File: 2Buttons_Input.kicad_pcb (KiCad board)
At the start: 2 copper layers, 46.2 x 30.2 mm, 19 parts, among them J1 JST_SH_SM06B-SRSS-TB_1x06-1MP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, SW1 SW_Push, SW2 SW_Push, U1 M24C02-FMN

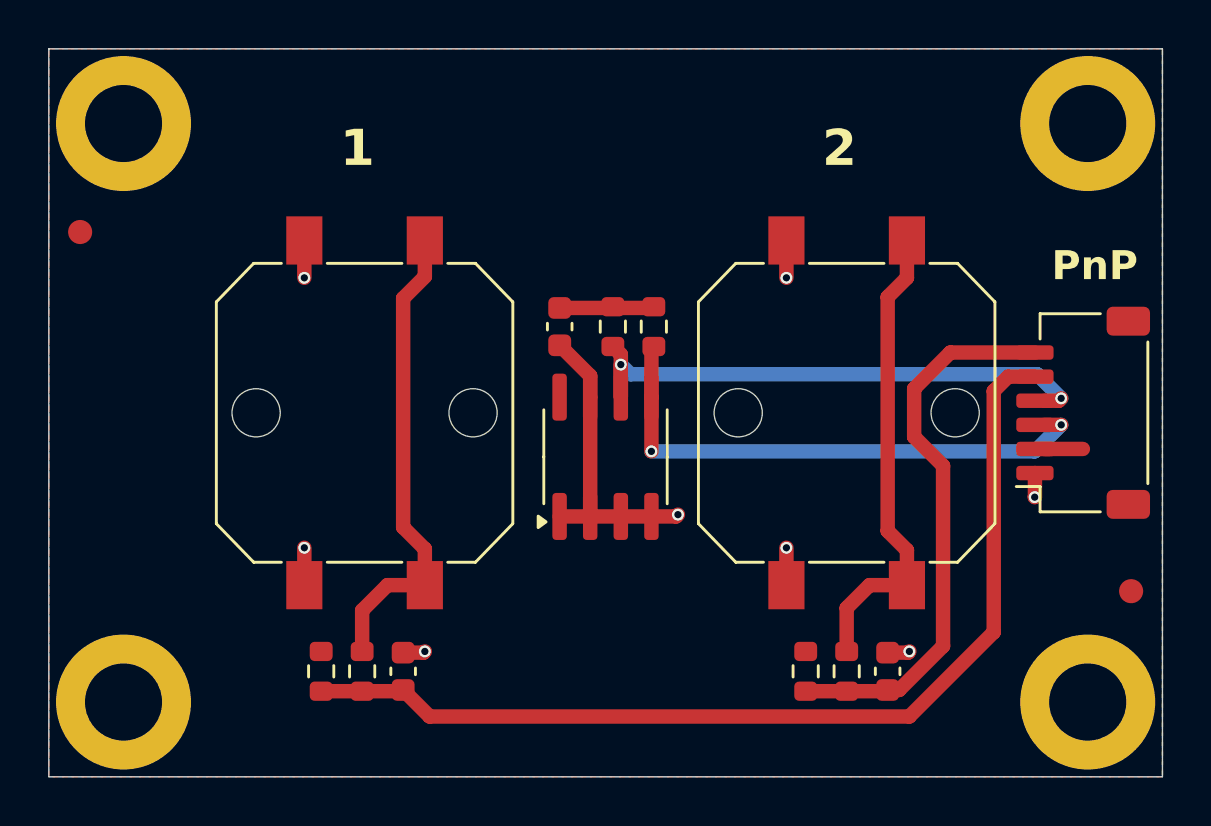
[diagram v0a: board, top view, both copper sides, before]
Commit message: Changing the button names on silk level to 0 and 1
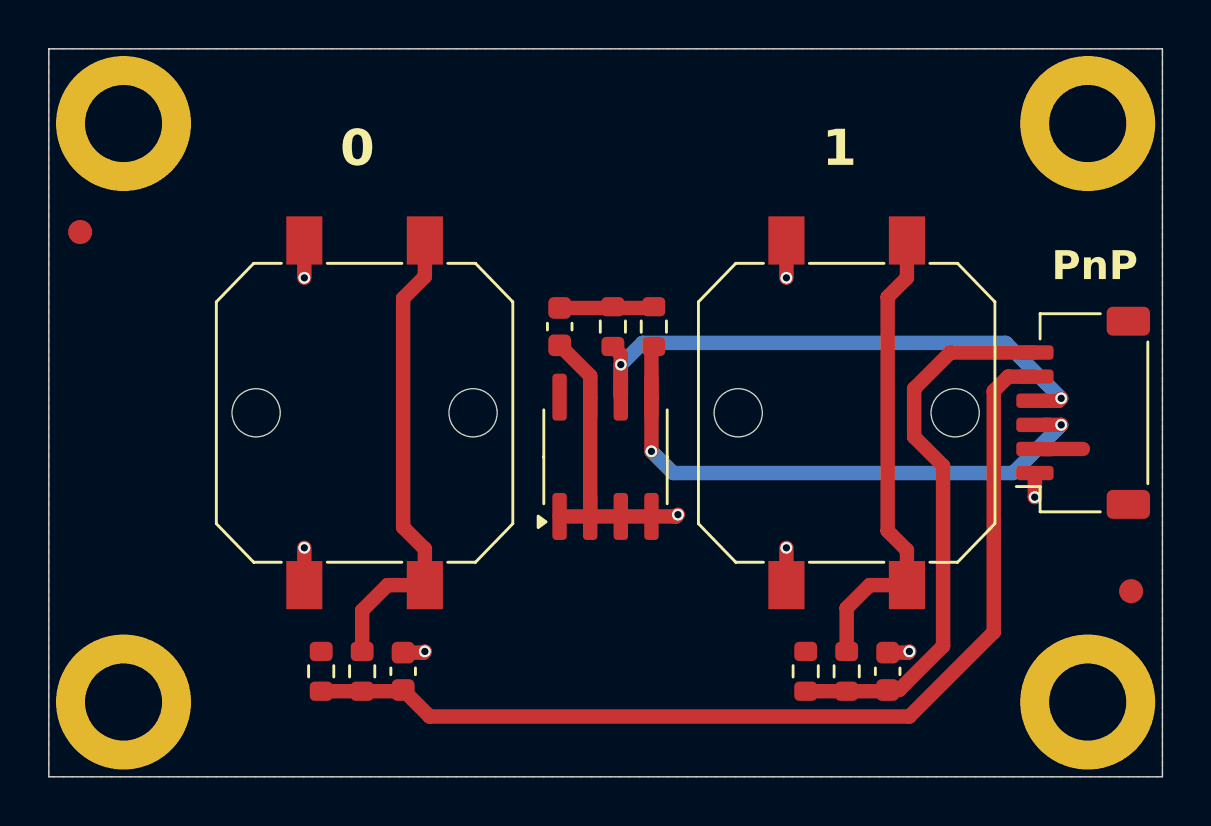
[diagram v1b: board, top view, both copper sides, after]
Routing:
- net SDA: track 22.5 -> 23.3 mm
- net SCL: track 23.2 -> 23.9 mm
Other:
- board text added: "0"
- board text removed: "2"
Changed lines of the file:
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@@
 	(paper "A5")
 	(title_block
-		(title "PlugAndPlay QWIIC adapter")
+		(title "PlugAndPlay 2 Buttons Input")
 		(date "2025-05-18")
 		(rev "2")
@@
 		(allow_soldermask_bridges_in_footprints no)
 		(pcbplotparams
-			(layerselection 0x00010fc_ffffffff)
+			(layerselection 0x00012fc_ffffffff)
 			(plot_on_all_layers_selection 0x0000000_00000000)
 			(disableapertmacros no)
-			(usegerberextensions yes)
-			(usegerberattributes yes)
+			(usegerberextensions no)
+			(usegerberattributes no)
 			(usegerberadvancedattributes yes)
 			(creategerberjobfile no)
@@
 		)
 	)
-	(gr_text "1"
+	(gr_text "0"
 		(at 32.585715 37 0)
 		(layer "F.SilkS")
@@
 		)
 	)
-	(gr_text "2"
+	(gr_text "1"
 		(at 52.585715 37 0)
 		(layer "F.SilkS")
@@
 	)
 	(segment
-		(start 61.4 48.7)
+		(start 46.4 49.6)
 		(end 45.5 48.7)
 		(width 0.6)
@@
 	)
 	(segment
+		(start 60.5 49.6)
+		(end 46.4 49.6)
+		(width 0.6)
+		(layer "B.Cu")
+		(net 4)
+	)
+	(segment
 		(start 62.5 47.6)
-		(end 61.4 48.7)
+		(end 60.5 49.6)
 		(width 0.6)
 		(layer "B.Cu")
@@
 	)
 	(segment
-		(start 44.63 45.5)
-		(end 44.23 45.1)
+		(start 60.2 44.2)
+		(end 45.13 44.2)
 		(width 0.6)
 		(layer "B.Cu")
@@
 	)
 	(segment
-		(start 62.5 46.5)
-		(end 61.5 45.5)
+		(start 45.13 44.2)
+		(end 44.23 45.1)
 		(width 0.6)
 		(layer "B.Cu")
@@
 	)
 	(segment
-		(start 61.5 45.5)
-		(end 44.63 45.5)
+		(start 62.5 46.5)
+		(end 60.2 44.2)
 		(width 0.6)
 		(layer "B.Cu")
